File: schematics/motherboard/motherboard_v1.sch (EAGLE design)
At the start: 65 parts, among them IC1 3.3V, SW1 A6H2101, Y1 25MHz

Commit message: Motherboard update with almost-ready routing
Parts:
- added H1, H2, H3, H4: MOUNT-PAD-ROUND3.0, holes:MOUNT-PAD-ROUND3.0
- added U$2: SKIPPYTXT-PLC-10MM, skippy-logo:SKIPPYTXT-PLC-10MM
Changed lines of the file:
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@@
 <setting verticaltext="up"/>
 </settings>
-<grid distance="0.1" unitdist="inch" unit="inch" style="dots" multiple="1" display="yes" altdistance="0.01" altunitdist="inch" altunit="inch"/>
+<grid distance="0.1" unitdist="inch" unit="inch" style="lines" multiple="1" display="yes" altdistance="0.01" altunitdist="inch" altunit="inch"/>
 <layers>
-<layer number="1" name="Top" color="4" fill="1" visible="yes" active="no"/>
-<layer number="16" name="Bottom" color="1" fill="1" visible="yes" active="no"/>
-<layer number="17" name="Pads" color="2" fill="1" visible="yes" active="no"/>
-<layer number="18" name="Vias" color="2" fill="1" visible="yes" active="no"/>
-<layer number="19" name="Unrouted" color="6" fill="1" visible="yes" active="no"/>
-<layer number="20" name="Dimension" color="15" fill="1" visible="yes" active="no"/>
-<layer number="21" name="tPlace" color="7" fill="1" visible="yes" active="no"/>
-<layer number="22" name="bPlace" color="7" fill="1" visible="yes" active="no"/>
-<layer number="23" name="tOrigins" color="15" fill="1" visible="yes" active="no"/>
-<layer number="24" name="bOrigins" color="15" fill="1" visible="yes" active="no"/>
-<layer number="25" name="tNames" color="7" fill="1" visible="yes" active="no"/>
-<layer number="26" name="bNames" color="7" fill="1" visible="yes" active="no"/>
-<layer number="27" name="tValues" color="7" fill="1" visible="yes" active="no"/>
-<layer number="28" name="bValues" color="7" fill="1" visible="yes" active="no"/>
+<layer number="1" name="Top" color="4" fill="1" visible="no" active="no"/>
+<layer number="16" name="Bottom" color="1" fill="1" visible="no" active="no"/>
+<layer number="17" name="Pads" color="2" fill="1" visible="no" active="no"/>
+<layer number="18" name="Vias" color="2" fill="1" visible="no" active="no"/>
+<layer number="19" name="Unrouted" color="6" fill="1" visible="no" active="no"/>
+<layer number="20" name="Dimension" color="15" fill="1" visible="no" active="no"/>
+<layer number="21" name="tPlace" color="7" fill="1" visible="no" active="no"/>
+<layer number="22" name="bPlace" color="7" fill="1" visible="no" active="no"/>
+<layer number="23" name="tOrigins" color="15" fill="1" visible="no" active="no"/>
+<layer number="24" name="bOrigins" color="15" fill="1" visible="no" active="no"/>
+<layer number="25" name="tNames" color="7" fill="1" visible="no" active="no"/>
+<layer number="26" name="bNames" color="7" fill="1" visible="no" active="no"/>
+<layer number="27" name="tValues" color="7" fill="1" visible="no" active="no"/>
+<layer number="28" name="bValues" color="7" fill="1" visible="no" active="no"/>
 <layer number="29" name="tStop" color="7" fill="3" visible="no" active="no"/>
 <layer number="30" name="bStop" color="7" fill="6" visible="no" active="no"/>
@@
 <layer number="35" name="tGlue" color="7" fill="4" visible="no" active="no"/>
 <layer number="36" name="bGlue" color="7" fill="5" visible="no" active="no"/>
-<layer number="37" name="tTest" color="7" fill="1" visible="yes" active="no"/>
-<layer number="38" name="bTest" color="7" fill="1" visible="yes" active="no"/>
+<layer number="37" name="tTest" color="7" fill="1" visible="no" active="no"/>
+<layer number="38" name="bTest" color="7" fill="1" visible="no" active="no"/>
 <layer number="39" name="tKeepout" color="4" fill="11" visible="no" active="no"/>
 <layer number="40" name="bKeepout" color="1" fill="11" visible="no" active="no"/>
@@
 <layer number="44" name="Drills" color="7" fill="1" visible="no" active="no"/>
 <layer number="45" name="Holes" color="7" fill="1" visible="no" active="no"/>
-<layer number="46" name="Milling" color="3" fill="1" visible="yes" active="no"/>
-<layer number="47" name="Measures" color="7" fill="1" visible="yes" active="no"/>
-<layer number="48" name="Document" color="7" fill="1" visible="yes" active="no"/>
-<layer number="49" name="Reference" color="7" fill="1" visible="yes" active="no"/>
-<layer number="50" name="dxf" color="7" fill="1" visible="yes" active="no"/>
-<layer number="51" name="tDocu" color="7" fill="1" visible="yes" active="no"/>
-<layer number="52" name="bDocu" color="7" fill="1" visible="yes" active="no"/>
-<layer number="53" name="tGND_GNDA" color="7" fill="9" visible="yes" active="no"/>
-<layer number="54" name="bGND_GNDA" color="1" fill="9" visible="yes" active="no"/>
-<layer number="56" name="wert" color="7" fill="1" visible="yes" active="no"/>
-<layer number="57" name="tCAD" color="7" fill="1" visible="yes" active="no"/>
+<layer number="46" name="Milling" color="3" fill="1" visible="no" active="no"/>
+<layer number="47" name="Measures" color="7" fill="1" visible="no" active="no"/>
+<layer number="48" name="Document" color="7" fill="1" visible="no" active="no"/>
+<layer number="49" name="Reference" color="7" fill="1" visible="no" active="no"/>
+<layer number="50" name="dxf" color="7" fill="1" visible="no" active="no"/>
+<layer number="51" name="tDocu" color="7" fill="1" visible="no" active="no"/>
+<layer number="52" name="bDocu" color="7" fill="1" visible="no" active="no"/>
+<layer number="53" name="tGND_GNDA" color="7" fill="9" visible="no" active="no"/>
+<layer number="54" name="bGND_GNDA" color="1" fill="9" visible="no" active="no"/>
+<layer number="56" name="wert" color="7" fill="1" visible="no" active="no"/>
+<layer number="57" name="tCAD" color="7" fill="1" visible="no" active="no"/>
 <layer number="90" name="Modules" color="5" fill="1" visible="yes" active="yes"/>
 <layer number="91" name="Nets" color="2" fill="1" visible="yes" active="yes"/>
@@
 <part name="SUPPLY12" library="SparkFun-Aesthetics" deviceset="VDD" device=""/>
 <part name="GND16" library="SparkFun-Aesthetics" deviceset="GND" device=""/>
+<part name="U$2" library="skippy-logo" deviceset="SKIPPYTXT-PLC-10MM" device=""/>
+<part name="H1" library="holes" deviceset="MOUNT-PAD-ROUND" device="3.0"/>
+<part name="H2" library="holes" deviceset="MOUNT-PAD-ROUND" device="3.0"/>
+<part name="H3" library="holes" deviceset="MOUNT-PAD-ROUND" device="3.0"/>
+<part name="H4" library="holes" deviceset="MOUNT-PAD-ROUND" device="3.0"/>
 </parts>
 <sheets>
@@
 <instance part="SUPPLY12" gate="VDD" x="193.04" y="43.18"/>
 <instance part="GND16" gate="1" x="193.04" y="25.4"/>
+<instance part="U$2" gate="G$1" x="259.08" y="83.82"/>
+<instance part="H1" gate="G$1" x="200.66" y="88.9"/>
+<instance part="H2" gate="G$1" x="200.66" y="81.28"/>
+<instance part="H3" gate="G$1" x="226.06" y="91.44"/>
+<instance part="H4" gate="G$1" x="226.06" y="83.82"/>
 </instances>
 <busses>

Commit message: Motherboard v1 RTM
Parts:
- added JP5: JUMPER-3SMD, SparkFun-Retired:JUMPER-3SMD
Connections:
- new net N$14: JP10.+
- new net N$16: JP12.+
- new net N$17: JP14.+
- new net N$18: JP13.+
- new net VCCIO: JP15.+, JP16.+, JP17.+, JP18.+, JP5.2
- net 3.3V: now also JP5.3; no longer JP10.+, JP12.+, JP13.+, JP14.+, JP15.+, JP16.+, JP17.+, JP18.+
- net PWM5: now also JP17.PWM, U$1.PC8; no longer JP15.PWM, U$1.PC6
- net PWM6: now also JP15.PWM, U$1.PC6; no longer JP16.PWM, U$1.PC7
- net PWM7: now also JP16.PWM, U$1.PC7; no longer JP17.PWM, U$1.PC8
- net VDD: now also JP5.1

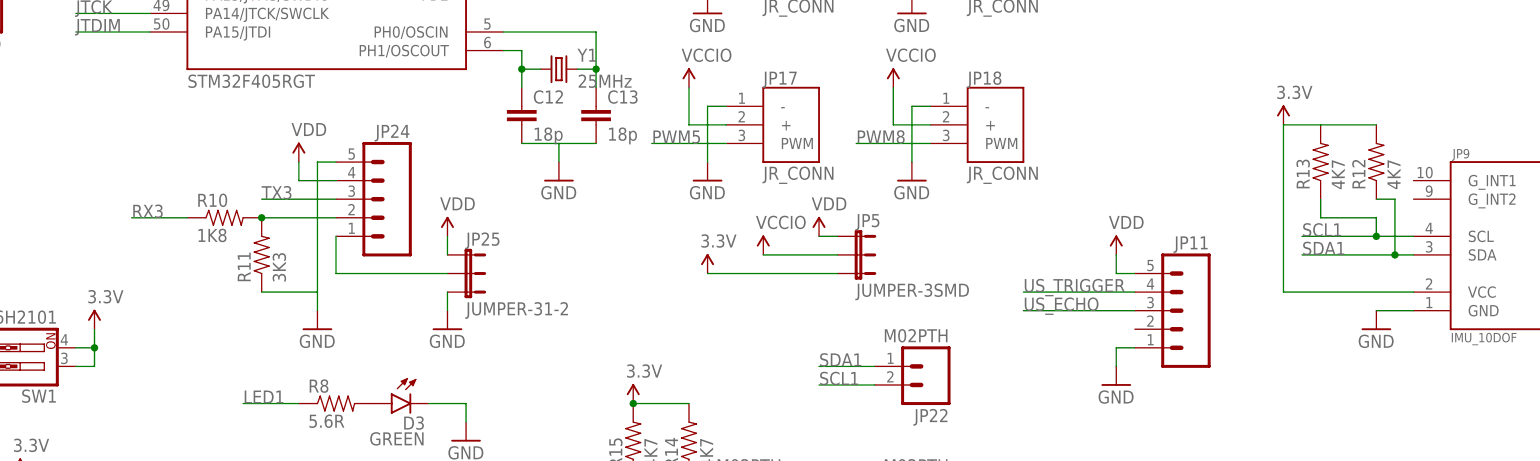
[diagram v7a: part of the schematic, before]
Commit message: Fixes issues #1 and #2
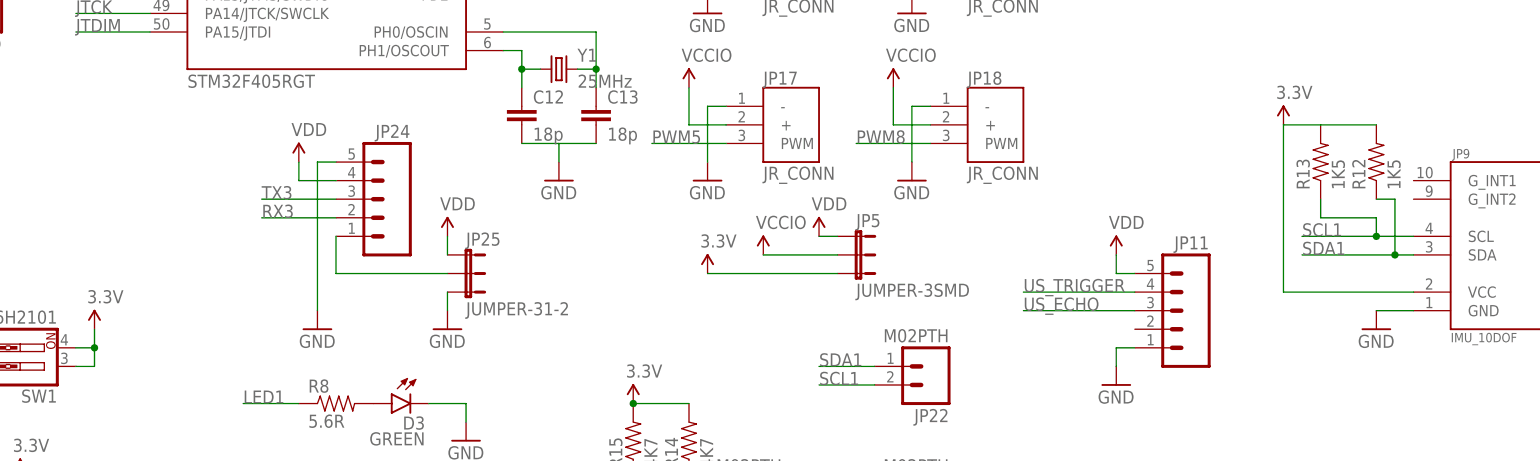
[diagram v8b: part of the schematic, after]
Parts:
- removed R10: 1K8, SparkFun-Resistors:RESISTOR1206
- removed R11: 3K3, SparkFun-Resistors:RESISTOR1206
- R12, R13: value 4K7 -> 1K5
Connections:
- removed net N$12: JP24.2, R10.2, R11.2
- net GND: no longer R11.1
- net RX3: now also JP24.2; no longer R10.1
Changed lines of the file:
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@@
 <?xml version="1.0" encoding="utf-8"?>
 <!DOCTYPE eagle SYSTEM "eagle.dtd">
-<eagle version="6.5.0">
+<eagle version="7.2.0">
 <drawing>
 <settings>
@@
 <grid distance="0.1" unitdist="inch" unit="inch" style="lines" multiple="1" display="no" altdistance="0.01" altunitdist="inch" altunit="inch"/>
 <layers>
-<layer number="1" name="Top" color="4" fill="1" visible="yes" active="no"/>
-<layer number="16" name="Bottom" color="1" fill="1" visible="yes" active="no"/>
-<layer number="17" name="Pads" color="2" fill="1" visible="yes" active="no"/>
-<layer number="18" name="Vias" color="2" fill="1" visible="yes" active="no"/>
-<layer number="19" name="Unrouted" color="6" fill="1" visible="yes" active="no"/>
-<layer number="20" name="Dimension" color="15" fill="1" visible="yes" active="no"/>
-<layer number="21" name="tPlace" color="7" fill="1" visible="yes" active="no"/>
-<layer number="22" name="bPlace" color="7" fill="1" visible="yes" active="no"/>
-<layer number="23" name="tOrigins" color="15" fill="1" visible="yes" active="no"/>
-<layer number="24" name="bOrigins" color="15" fill="1" visible="yes" active="no"/>
-<layer number="25" name="tNames" color="7" fill="1" visible="yes" active="no"/>
-<layer number="26" name="bNames" color="7" fill="1" visible="yes" active="no"/>
-<layer number="27" name="tValues" color="7" fill="1" visible="yes" active="no"/>
-<layer number="28" name="bValues" color="7" fill="1" visible="yes" active="no"/>
+<layer number="1" name="Top" color="4" fill="1" visible="no" active="no"/>
+<layer number="16" name="Bottom" color="1" fill="1" visible="no" active="no"/>
+<layer number="17" name="Pads" color="2" fill="1" visible="no" active="no"/>
+<layer number="18" name="Vias" color="2" fill="1" visible="no" active="no"/>
+<layer number="19" name="Unrouted" color="6" fill="1" visible="no" active="no"/>
+<layer number="20" name="Dimension" color="15" fill="1" visible="no" active="no"/>
+<layer number="21" name="tPlace" color="7" fill="1" visible="no" active="no"/>
+<layer number="22" name="bPlace" color="7" fill="1" visible="no" active="no"/>
+<layer number="23" name="tOrigins" color="15" fill="1" visible="no" active="no"/>
+<layer number="24" name="bOrigins" color="15" fill="1" visible="no" active="no"/>
+<layer number="25" name="tNames" color="7" fill="1" visible="no" active="no"/>
+<layer number="26" name="bNames" color="7" fill="1" visible="no" active="no"/>
+<layer number="27" name="tValues" color="7" fill="1" visible="no" active="no"/>
+<layer number="28" name="bValues" color="7" fill="1" visible="no" active="no"/>
 <layer number="29" name="tStop" color="7" fill="3" visible="no" active="no"/>
 <layer number="30" name="bStop" color="7" fill="6" visible="no" active="no"/>
@@
 <layer number="35" name="tGlue" color="7" fill="4" visible="no" active="no"/>
 <layer number="36" name="bGlue" color="7" fill="5" visible="no" active="no"/>
-<layer number="37" name="tTest" color="7" fill="1" visible="yes" active="no"/>
-<layer number="38" name="bTest" color="7" fill="1" visible="yes" active="no"/>
+<layer number="37" name="tTest" color="7" fill="1" visible="no" active="no"/>
+<layer number="38" name="bTest" color="7" fill="1" visible="no" active="no"/>
 <layer number="39" name="tKeepout" color="4" fill="11" visible="no" active="no"/>
 <layer number="40" name="bKeepout" color="1" fill="11" visible="no" active="no"/>
@@
 <layer number="44" name="Drills" color="7" fill="1" visible="no" active="no"/>
 <layer number="45" name="Holes" color="7" fill="1" visible="no" active="no"/>
-<layer number="46" name="Milling" color="3" fill="1" visible="yes" active="no"/>
-<layer number="47" name="Measures" color="7" fill="1" visible="yes" active="no"/>
-<layer number="48" name="Document" color="7" fill="1" visible="yes" active="no"/>
-<layer number="49" name="Reference" color="7" fill="1" visible="yes" active="no"/>
-<layer number="50" name="dxf" color="7" fill="1" visible="yes" active="no"/>
-<layer number="51" name="tDocu" color="7" fill="1" visible="yes" active="no"/>
-<layer number="52" name="bDocu" color="7" fill="1" visible="yes" active="no"/>
-<layer number="53" name="tGND_GNDA" color="7" fill="9" visible="yes" active="no"/>
-<layer number="54" name="bGND_GNDA" color="1" fill="9" visible="yes" active="no"/>
-<layer number="56" name="wert" color="7" fill="1" visible="yes" active="no"/>
-<layer number="57" name="tCAD" color="7" fill="1" visible="yes" active="no"/>
+<layer number="46" name="Milling" color="3" fill="1" visible="no" active="no"/>
+<layer number="47" name="Measures" color="7" fill="1" visible="no" active="no"/>
+<layer number="48" name="Document" color="7" fill="1" visible="no" active="no"/>
+<layer number="49" name="Reference" color="7" fill="1" visible="no" active="no"/>
+<layer number="50" name="dxf" color="7" fill="1" visible="no" active="no"/>
+<layer number="51" name="tDocu" color="7" fill="1" visible="no" active="no"/>
+<layer number="52" name="bDocu" color="7" fill="1" visible="no" active="no"/>
+<layer number="53" name="tGND_GNDA" color="7" fill="9" visible="no" active="no"/>
+<layer number="54" name="bGND_GNDA" color="1" fill="9" visible="no" active="no"/>
+<layer number="56" name="wert" color="7" fill="1" visible="no" active="no"/>
+<layer number="57" name="tCAD" color="7" fill="1" visible="no" active="no"/>
 <layer number="90" name="Modules" color="5" fill="1" visible="yes" active="yes"/>
 <layer number="91" name="Nets" color="2" fill="1" visible="yes" active="yes"/>
@@
 <part name="GND29" library="SparkFun-Aesthetics" deviceset="GND" device=""/>
 <part name="SUPPLY26" library="SparkFun-Aesthetics" deviceset="VDD" device=""/>
-<part name="R10" library="SparkFun-Resistors" deviceset="RESISTOR" device="1206" value="1K8"/>
-<part name="R11" library="SparkFun-Resistors" deviceset="RESISTOR" device="1206" value="3K3"/>
 <part name="JP25" library="SparkFun-Retired" deviceset="JUMPER-3" device="1-2"/>
 <part name="SUPPLY27" library="SparkFun-Aesthetics" deviceset="VDD" device=""/>
 <part name="GND30" library="SparkFun-Aesthetics" deviceset="GND" device=""/>
-<part name="R12" library="SparkFun-Resistors" deviceset="RESISTOR" device="1206" value="4K7"/>
-<part name="R13" library="SparkFun-Resistors" deviceset="RESISTOR" device="1206" value="4K7"/>
+<part name="R12" library="SparkFun-Resistors" deviceset="RESISTOR" device="1206" value="1K5"/>
+<part name="R13" library="SparkFun-Resistors" deviceset="RESISTOR" device="1206" value="1K5"/>
 <part name="SUPPLY28" library="SparkFun-Aesthetics" deviceset="3.3V" device=""/>
 <part name="R14" library="SparkFun-Resistors" deviceset="RESISTOR" device="1206" value="4K7"/>
@@
 <instance part="GND29" gate="1" x="83.82" y="33.02"/>
 <instance part="SUPPLY26" gate="VDD" x="81.28" y="55.88"/>
-<instance part="R10" gate="G$1" x="71.12" y="48.26"/>
-<instance part="R11" gate="G$1" x="76.2" y="43.18" rot="R90"/>
 <instance part="JP25" gate="G$1" x="104.14" y="43.18" rot="R270"/>
 <instance part="SUPPLY27" gate="VDD" x="101.6" y="45.72"/>
@@
 <pinref part="GND29" gate="1" pin="GND"/>
 <wire x1="86.36" y1="55.88" x2="83.82" y2="55.88" width="0.1524" layer="91"/>
-<wire x1="83.82" y1="55.88" x2="83.82" y2="38.1" width="0.1524" layer="91"/>
-<pinref part="R11" gate="G$1" pin="1"/>
-<wire x1="83.82" y1="38.1" x2="83.82" y2="35.56" width="0.1524" layer="91"/>
-<wire x1="76.2" y1="38.1" x2="83.82" y2="38.1" width="0.1524" layer="91"/>
+<wire x1="83.82" y1="55.88" x2="83.82" y2="35.56" width="0.1524" layer="91"/>
 </segment>
 <segment>
@@
 </segment>
 <segment>
-<pinref part="R10" gate="G$1" pin="1"/>
-<wire x1="66.04" y1="48.26" x2="58.42" y2="48.26" width="0.1524" layer="91"/>
-<label x="58.42" y="48.26" size="1.778" layer="95"/>
+<label x="76.2" y="48.26" size="1.778" layer="95"/>
+<pinref part="JP24" gate="G$1" pin="2"/>
+<wire x1="76.2" y1="48.26" x2="86.36" y2="48.26" width="0.1524" layer="91"/>
 </segment>
 </net>
@@
 </segment>
 </net>
-<net name="N$12" class="0">
-<segment>
-<pinref part="R10" gate="G$1" pin="2"/>
-<pinref part="JP24" gate="G$1" pin="2"/>
-<wire x1="76.2" y1="48.26" x2="86.36" y2="48.26" width="0.1524" layer="91"/>
-<pinref part="R11" gate="G$1" pin="2"/>
-<junction x="76.2" y="48.26"/>
-</segment>
-</net>
